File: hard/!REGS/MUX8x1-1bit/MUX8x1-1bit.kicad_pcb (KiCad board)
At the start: 2 copper layers, 129.5 x 39.4 mm, 22 parts, among them J1 Conn_01x01_Male, J10 Conn_01x01_Male, J11 Conn_01x01_Male, J12 Conn_01x03_Male, J13 Conn_01x01_Male, J14 Conn_01x01_Male, J15 Conn_01x01_Male, J16 Conn_01x01_Male, J2 Conn_01x01_Male, J3 Conn_01x01_Male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

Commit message: MUX8x1-1bit v2 rework
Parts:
- moved J13 12.7 mm to (142.2, 49.5)
- moved J11 5.08 mm to (142.2, 36.8)
- moved J12 5.08 mm to (142.2, 44.5)
- renumbered J12 to J11, J13 to J12, J11 to J13
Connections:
- U1 pad 6: Net-(U1-Pad6) -> unconnected-(U1-~{Z}-Pad6)
- U2 pad 6: Net-(U2-Pad6) -> unconnected-(U2-~{Z}-Pad6)
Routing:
- net VCC: track 160.7 -> 131.1 mm, vias 2 -> 4
- net /O0: track 89.5 -> 106.7 mm
- net /S1.1: track 36.5 -> 34.3 mm
- net /S1.2: track 34.9 -> 32.7 mm
- net /S1.0: track 38.2 -> 36.6 mm
- net /S0.2: track 71.9 -> 70.7 mm
- net /S0.0: track 75.2 -> 76.1 mm
- net /~{E1}: track 35.9 -> 35.2 mm
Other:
- board text added: "28.03.26"
- board text removed: "27.03.26"

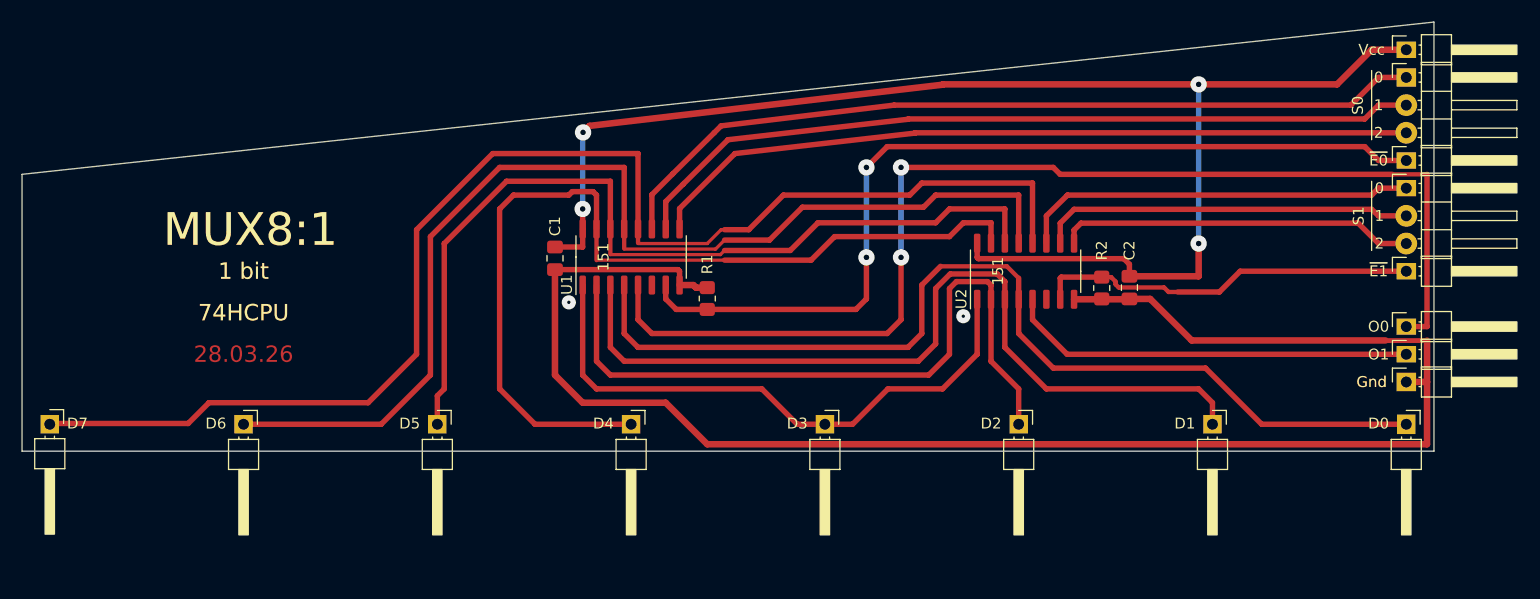
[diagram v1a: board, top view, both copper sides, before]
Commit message: MUX8x1-1bit v2 rework
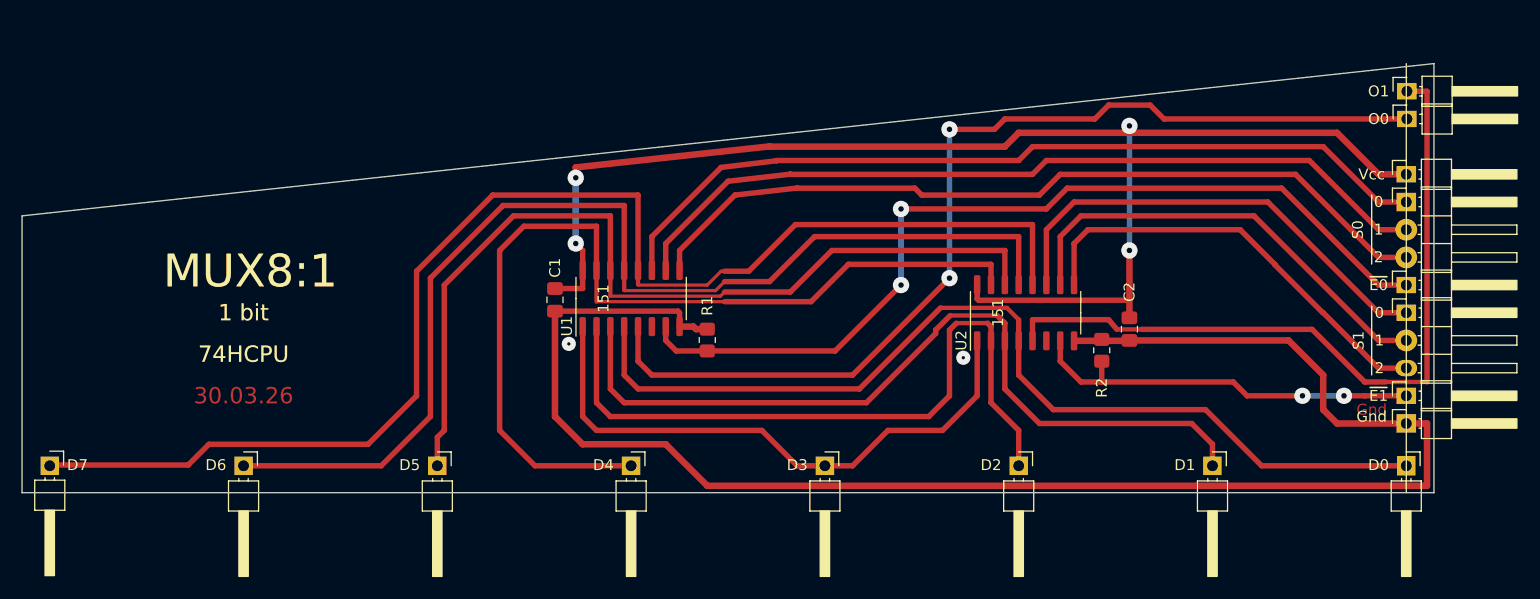
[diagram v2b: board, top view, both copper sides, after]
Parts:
- moved J14 24.1 mm to (142.3, 27.9)
- moved J13 19.1 mm to (142.3, 30.5)
- moved J15 11.4 mm to (142.2, 35.6)
- moved J10 11.4 mm to (142.2, 45.7)
- moved J11 11.4 mm to (142.2, 48.3)
- moved J12 11.4 mm to (142.2, 55.9)
- moved J9 11.4 mm to (142.2, 38.1)
- moved R2 5.71 mm to (114.3, 51.7), turned to 90 degrees
- moved C1 3.81 mm to (64.1, 47.1)
- moved C2 3.81 mm to (116.8, 49.8)
- moved J16 3.81 mm to (142.2, 58.4)
- moved R1 3.81 mm to (78.1, 50.8)
- moved J1 3.81 mm to (142.2, 62.3)
- moved J2 3.81 mm to (124.5, 62.3)
- moved J3 3.81 mm to (106.7, 62.3)
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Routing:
- net /O1: track 37.5 -> 69.1 mm
- net /O0: track 106.7 -> 93.0 mm
- net /S1.1: track 34.3 -> 41.7 mm
- net /S1.2: track 32.7 -> 40.1 mm
- net /S1.0: track 36.6 -> 43.3 mm
- net VCC: track 131.1 -> 125.4 mm
- net /S0.2: track 70.7 -> 74.9 mm
- net /D1: track 78.2 -> 75.4 mm
- net /D0: track 91.4 -> 88.8 mm
- net /S0.1: track 73.4 -> 76.0 mm
- net GND: track 153.1 -> 150.8 mm
- net /~{E1}: track 35.2 -> 36.8 mm, vias 0 -> 2
- net /S0.0: track 76.1 -> 77.6 mm
- net /D4: track 85.1 -> 86.1 mm
- net /D5: track 82.2 -> 83.1 mm
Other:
- board text added: "30.03.26"
- board text removed: "28.03.26"

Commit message: MUX8x1-1bit v2 is ready
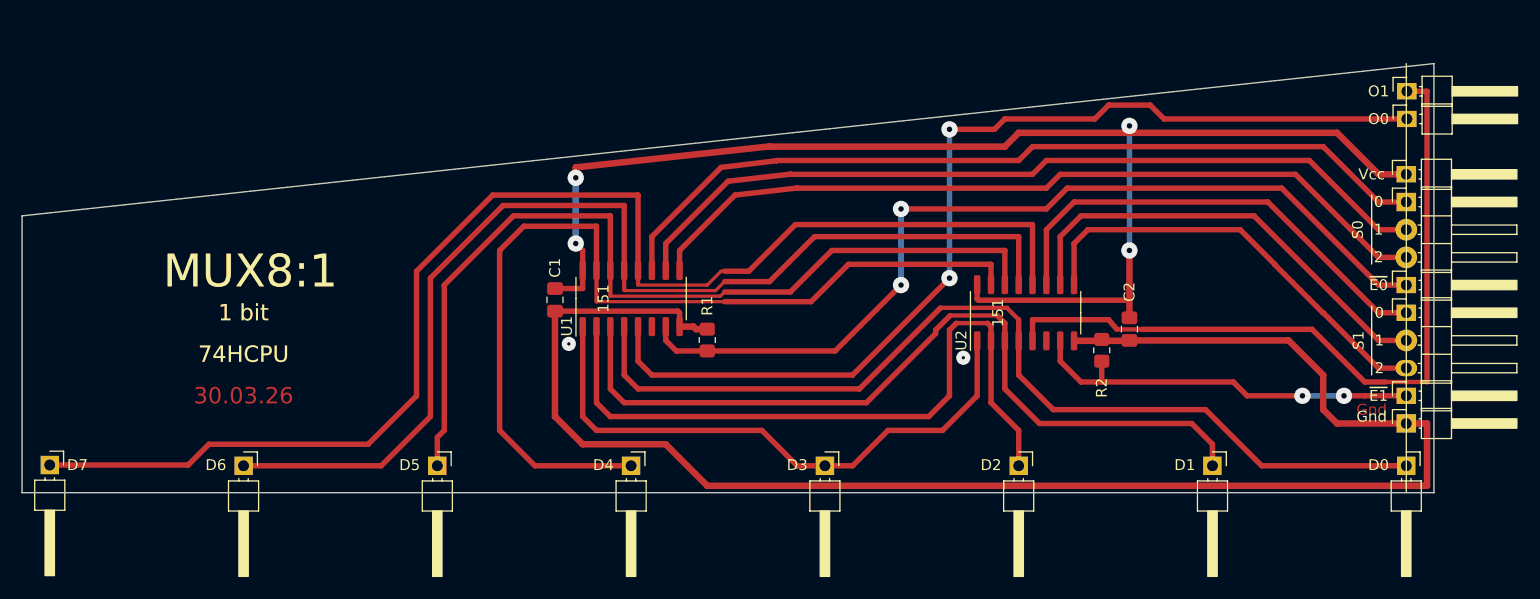
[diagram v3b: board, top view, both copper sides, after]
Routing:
- net /S0.2: track 74.9 -> 74.3 mm
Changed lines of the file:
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@@
 		)
 		(property "Value" "Conn_01x01_Male"
-			(at 1.778 -4.064 180)
+			(at 1.778 8.255 180)
 			(layer "F.Fab")
 			(effects
@@
 		(pad "1" thru_hole rect
 			(at 0 0 270)
-			(size 1.8 1.7)
+			(size 1.7 1.7)
 			(drill 1)
 			(layers "*.Cu" "*.Mask")
@@
 		)
 		(pad "1" thru_hole rect
-			(at 0.07 0 270)
+			(at 0 0 270)
 			(size 1.7 1.7)
 			(drill 1)
@@
 	)
 	(segment
-		(start 97.79 37.465)
-		(end 97.155 36.83)
-		(width 0.5)
-		(layer "F.Cu")
-		(net 11)
-	)
-	(segment
 		(start 86.36 36.815568)
-		(end 80.645 37.465)
+		(end 86.374432 36.83)
 		(width 0.5)
 		(layer "F.Cu")
@@
 	)
 	(segment
-		(start 132.08 35.56)
-		(end 110.49 35.56)
+		(start 86.374432 36.83)
+		(end 109.22 36.83)
 		(width 0.5)
 		(layer "F.Cu")
@@
 	)
 	(segment
-		(start 110.49 35.56)
-		(end 108.585 37.465)
+		(start 75.565 42.545)
+		(end 80.645 37.465)
 		(width 0.5)
 		(layer "F.Cu")
@@
 	)
 	(segment
-		(start 108.585 37.465)
-		(end 97.79 37.465)
+		(start 75.565 44.38)
+		(end 75.565 42.545)
 		(width 0.5)
 		(layer "F.Cu")
@@
 	)
 	(segment
-		(start 142.24 43.18)
+		(start 132.08 35.56)
 		(end 139.7 43.18)
 		(width 0.5)
@@
 	)
 	(segment
-		(start 86.374432 36.83)
-		(end 86.36 36.815568)
+		(start 139.7 43.18)
+		(end 142.24 43.18)
 		(width 0.5)
 		(layer "F.Cu")
@@
 	)
 	(segment
-		(start 80.645 37.465)
-		(end 75.565 42.545)
+		(start 109.22 36.83)
+		(end 110.49 35.56)
 		(width 0.5)
 		(layer "F.Cu")
@@
 	)
 	(segment
-		(start 139.7 43.18)
+		(start 110.49 35.56)
 		(end 132.08 35.56)
 		(width 0.5)
@@
 	)
 	(segment
-		(start 75.565 42.545)
-		(end 75.565 44.38)
-		(width 0.5)
-		(layer "F.Cu")
-		(net 11)
-	)
-	(segment
-		(start 97.155 36.83)
-		(end 86.374432 36.83)
+		(start 80.645 37.465)
+		(end 86.36 36.815568)
 		(width 0.5)
 		(layer "F.Cu")

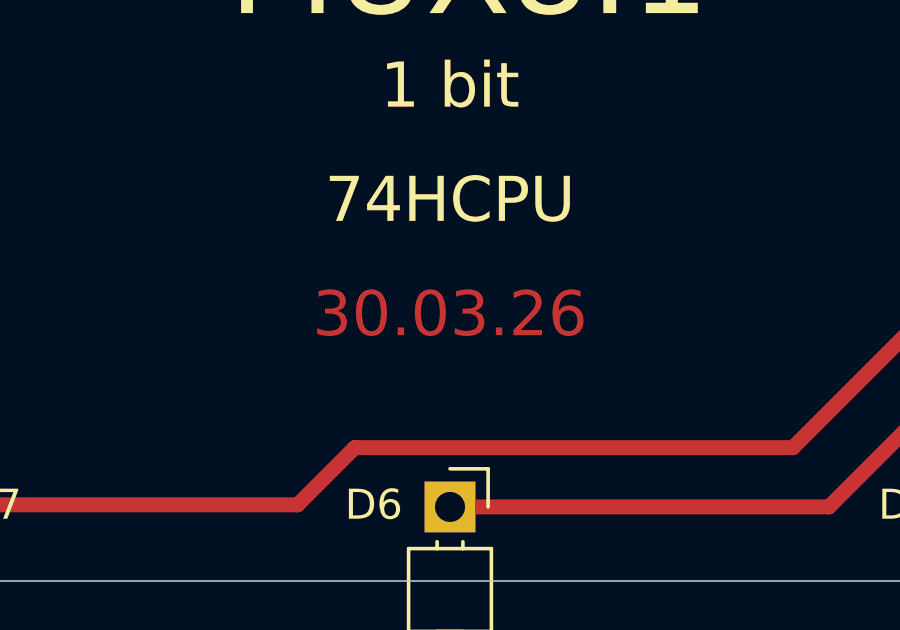
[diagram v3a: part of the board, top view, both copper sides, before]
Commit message: MUX8x1-1bit gerbers
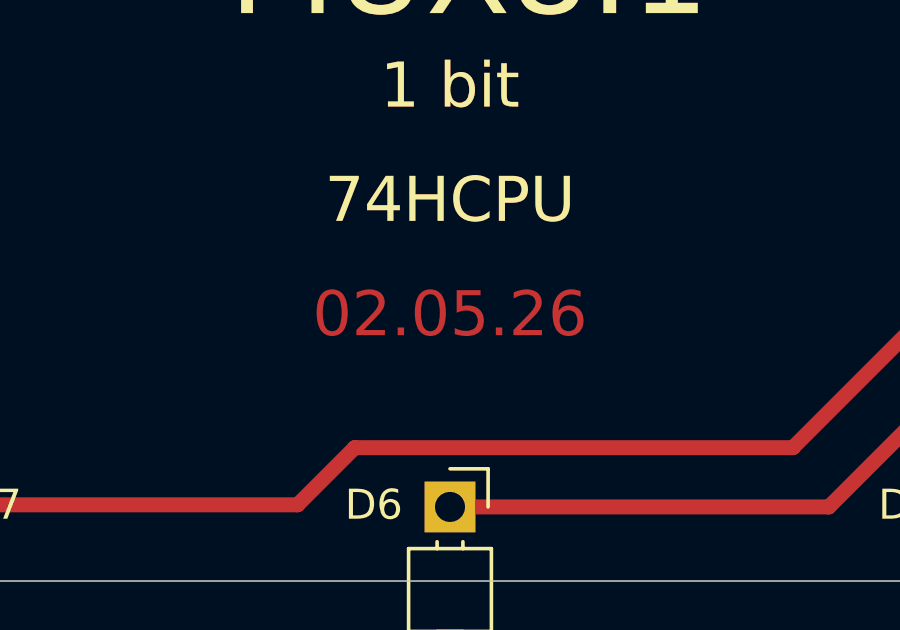
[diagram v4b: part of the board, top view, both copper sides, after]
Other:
- board text added: "02.05.26"
- board text removed: "30.03.26"
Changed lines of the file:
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@@
 		)
 	)
-	(gr_text "30.03.26"
+	(gr_text "02.05.26"
 		(at 35.56 55.88 0)
 		(layer "F.Cu")

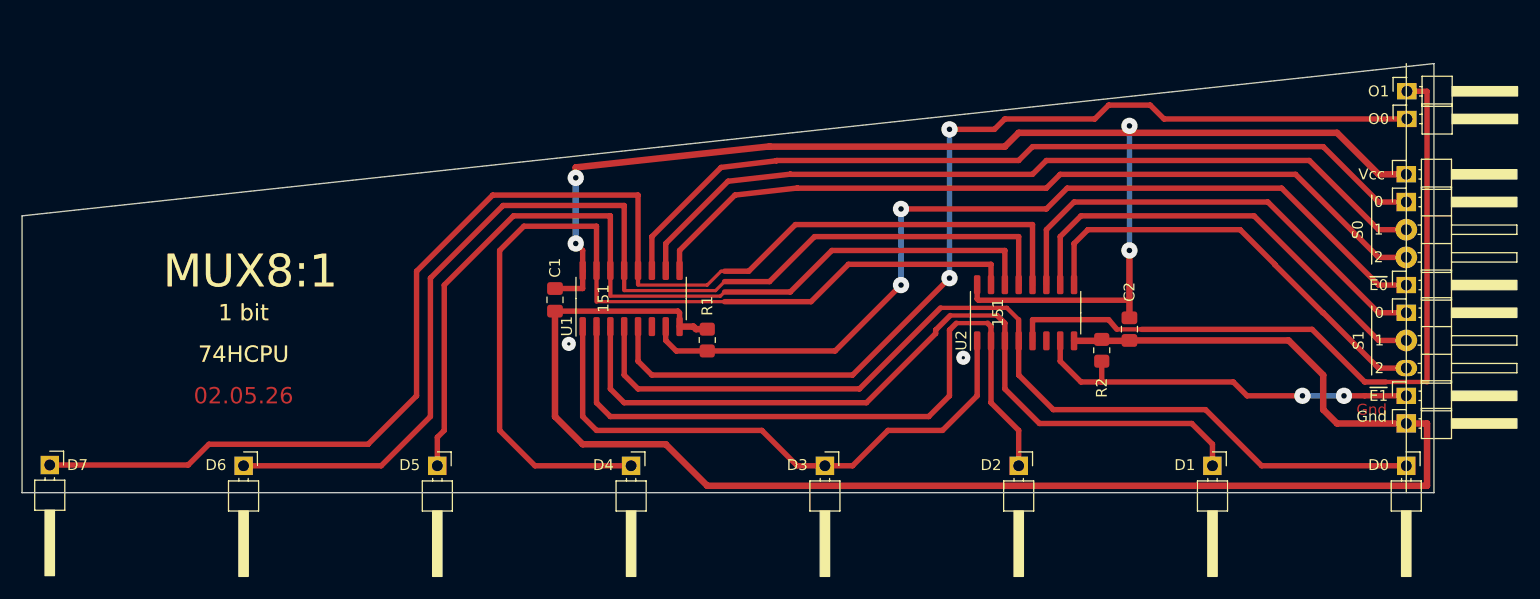
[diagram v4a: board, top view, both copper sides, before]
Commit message: Line on Silk is not required!
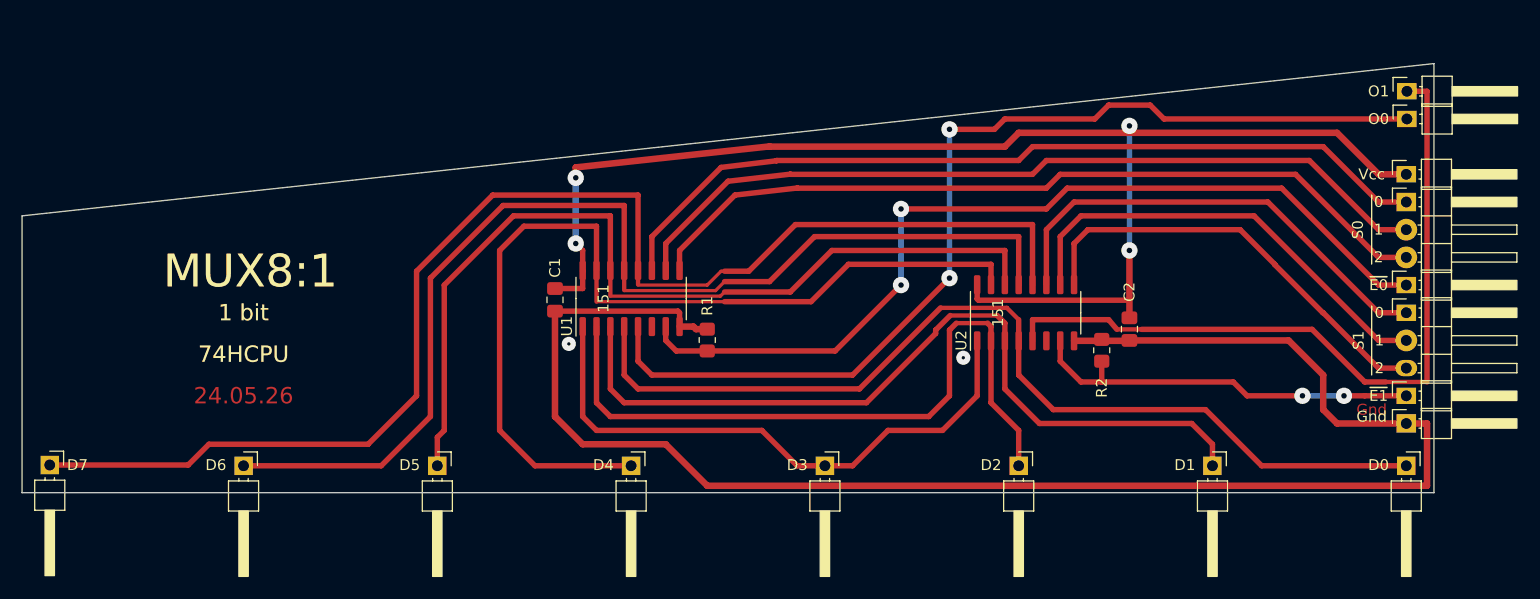
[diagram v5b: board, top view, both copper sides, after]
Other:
- board text added: "24.05.26"
- board text removed: "02.05.26"
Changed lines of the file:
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@@
-	)
-	(gr_line
-		(start 142.24 25.4)
-		(end 142.24 64.77)
-		(stroke
-			(width 0.12)
-			(type default)
-		)
-		(layer "F.SilkS")
 	)
 	(gr_line
@@
 		)
 	)
-	(gr_text "02.05.26"
+	(gr_text "24.05.26"
 		(at 35.56 55.88 0)
 		(layer "F.Cu")
